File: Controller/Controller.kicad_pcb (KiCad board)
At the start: 2 copper layers, 30 x 213 mm, 93 parts, among them J1 CON_TLC, J2 CON_15V, J3 CON_ICSP, J4 DC out, J5 CON_5V, J6 CON_5V_AUX, J7 CON_USB_A, Q1 SI4435FDY, Q2 SI4435FDY, Q3 SQ2309ES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

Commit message: ...
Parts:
- moved F2 31.6 mm to (138.0, 174.5), turned to 270 degrees
- moved Q2 22.1 mm to (144.5, 175.0), turned to 90 degrees
- moved C1 20.5 mm to (143.5, 197.0), turned to 180 degrees
- moved D2 18.2 mm to (149.0, 174.5), turned to 270 degrees
- moved D1 15.6 mm to (151.5, 214.5)
- moved Q1 15.6 mm to (153.5, 219.5)
- moved R1 15.6 mm to (155.6, 214.5)
- moved R2 14.5 mm to (149.0, 178.0), turned to 270 degrees
- moved C2 14.2 mm to (143.5, 208.5), turned to 180 degrees
- moved R13 14.0 mm to (158.0, 44.0), turned to 0 degrees
- moved SW1 12.9 mm to (147.0, 37.0), turned to 270 degrees
- moved J5 12.3 mm to (138.5, 183.5)
- moved U4 11.2 mm to (158.0, 41.0), turned to 270 degrees
- moved C4 9.92 mm to (155.0, 175.0), turned to 0 degrees
- moved C24 9.43 mm to (158.0, 38.0), turned to 0 degrees
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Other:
- outline, holes or cut-outs redrawn

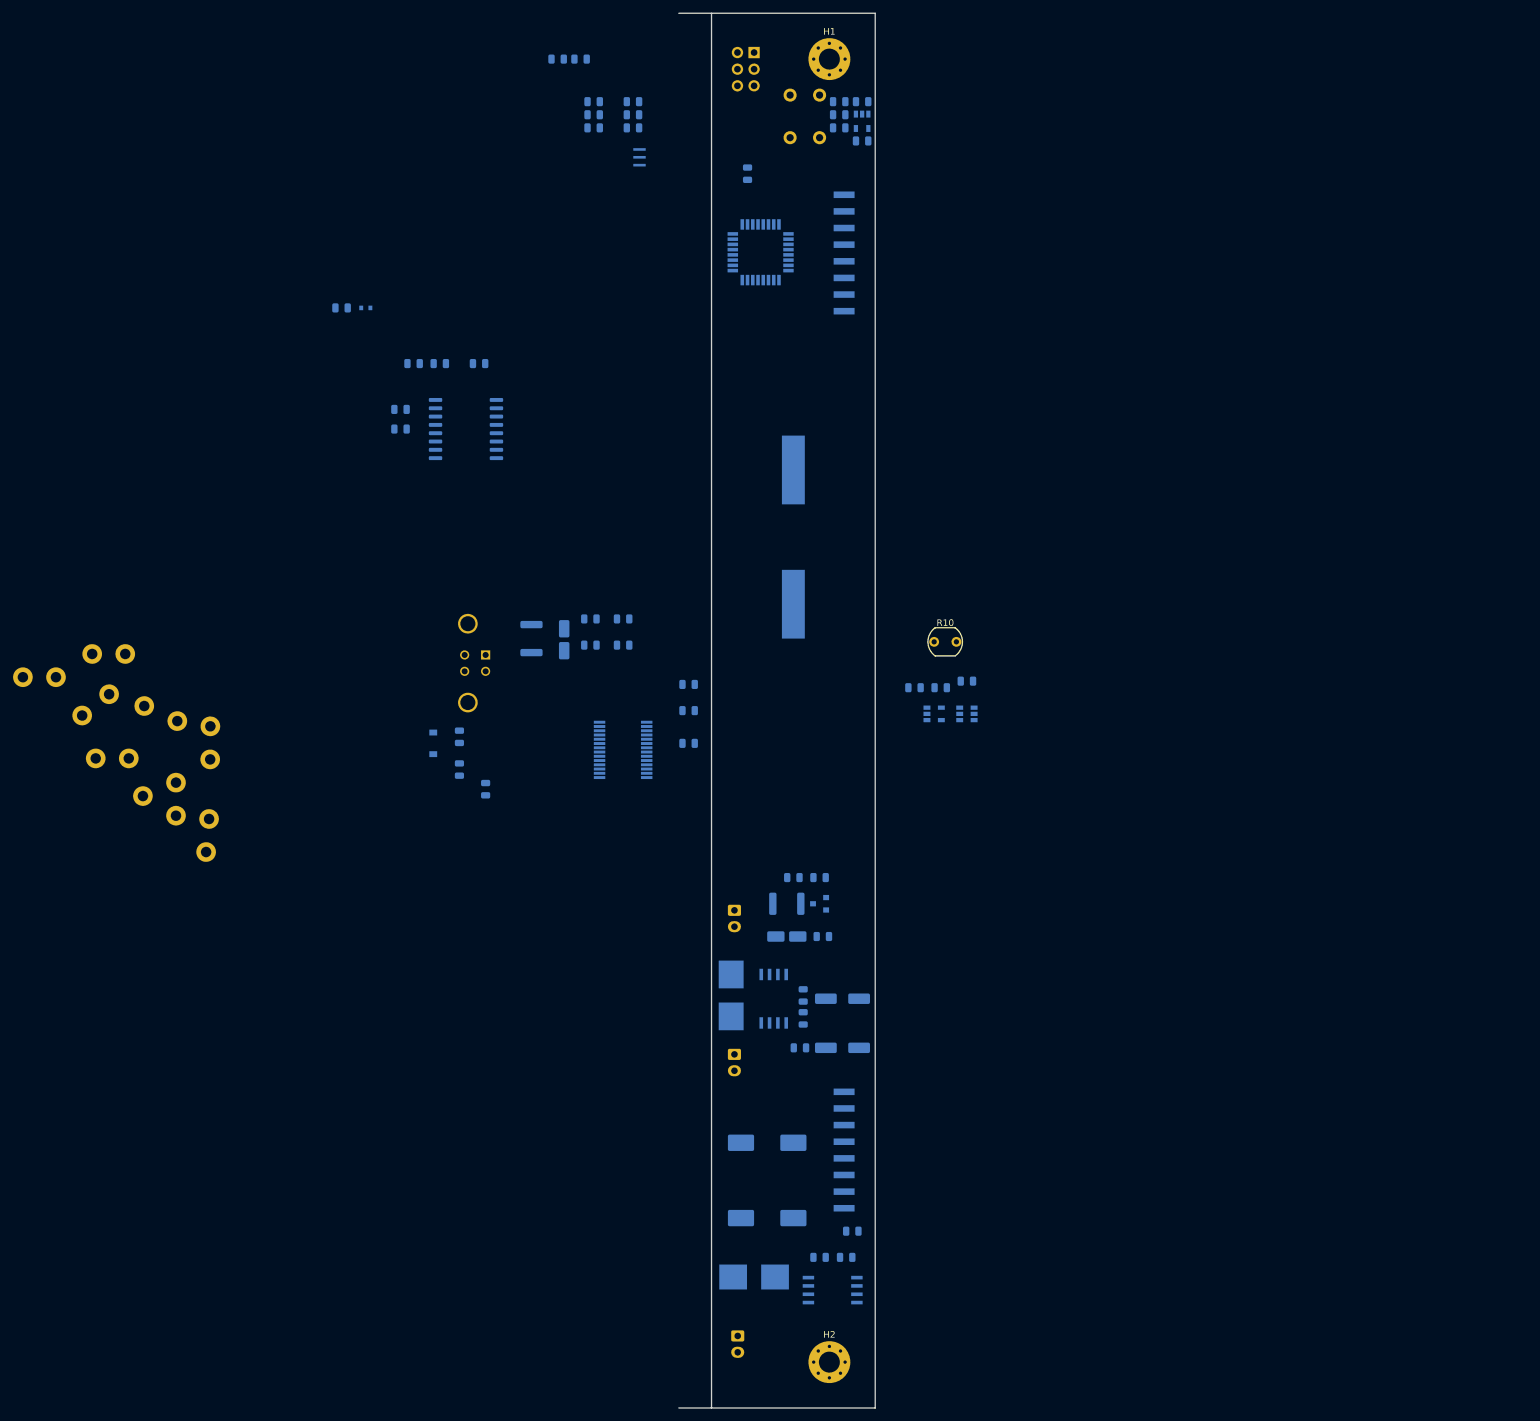
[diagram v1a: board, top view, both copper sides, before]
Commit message: Ground vias digit+colon. Placement/routing controller
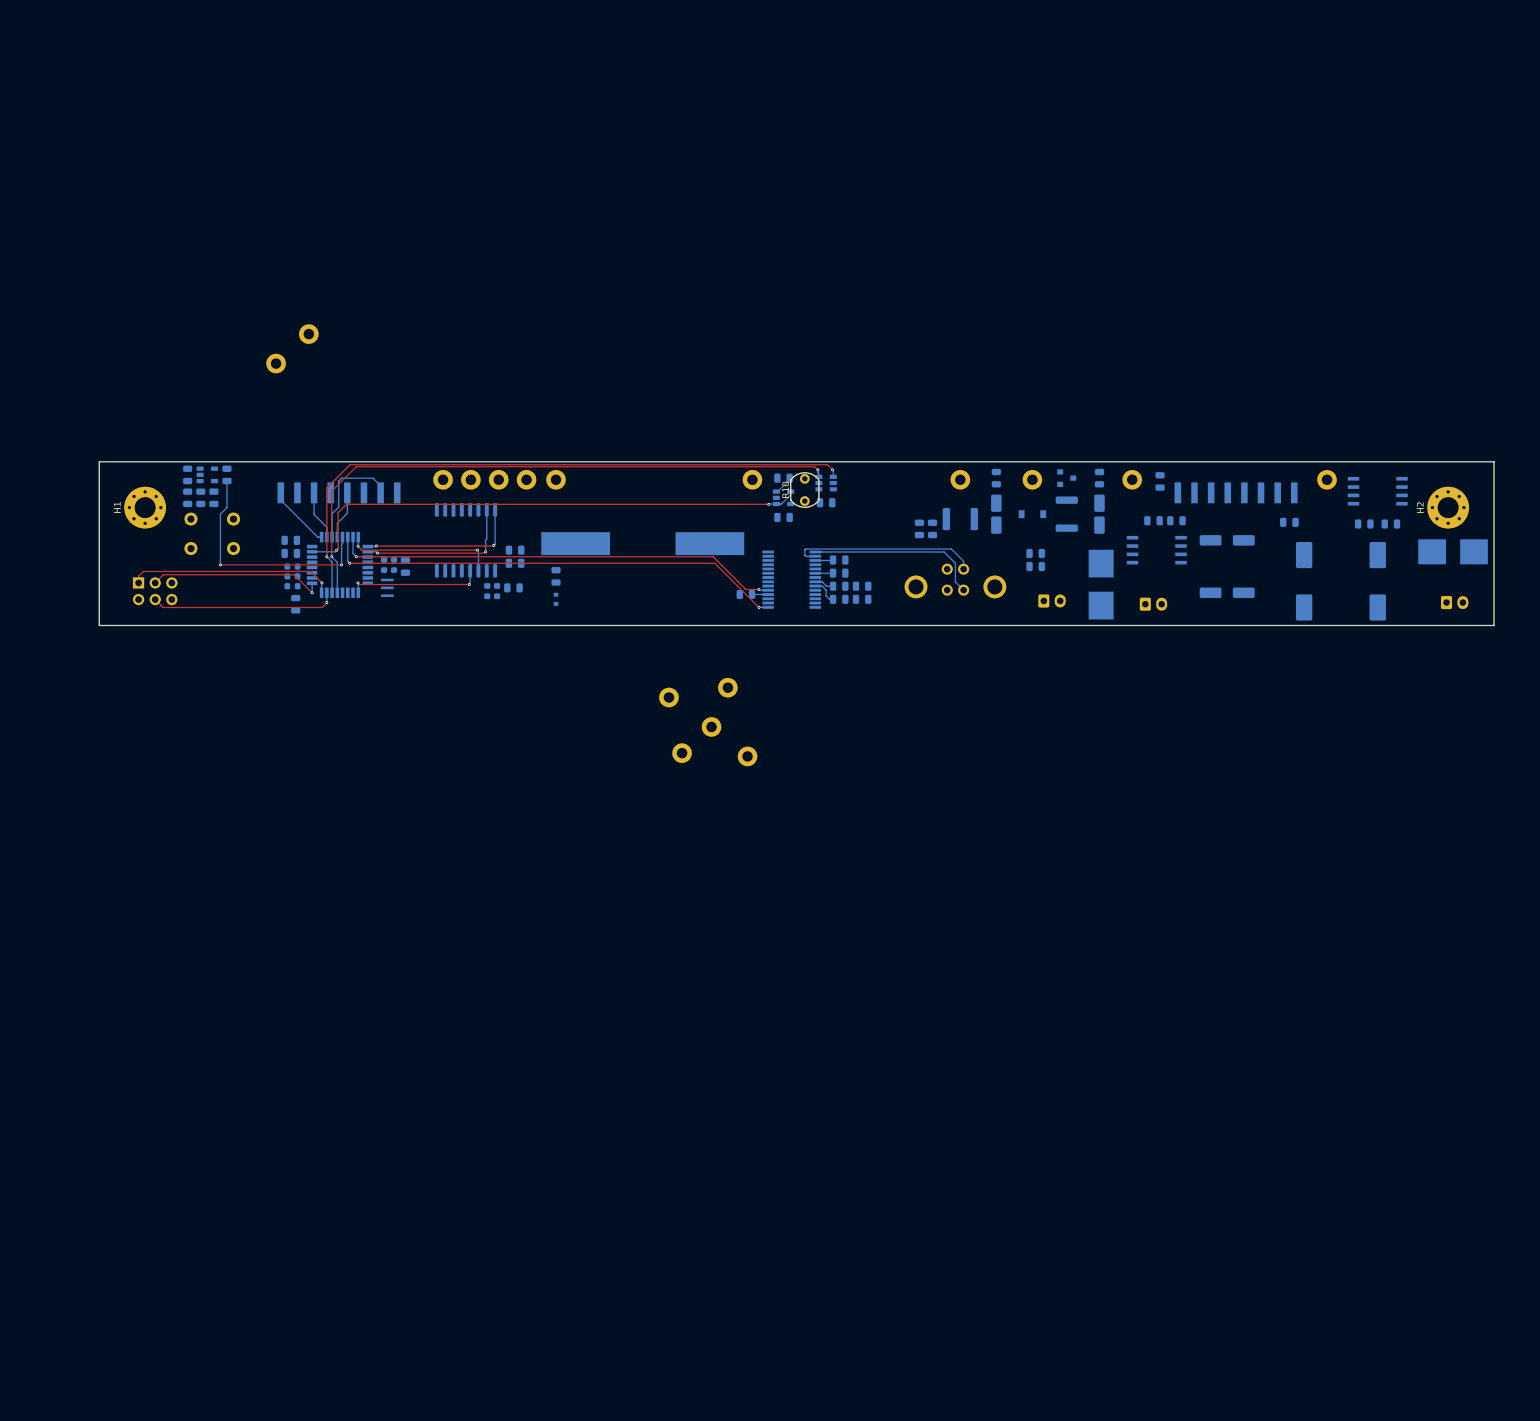
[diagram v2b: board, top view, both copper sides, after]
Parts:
- C14, C15, C16, C17, C18, C19, C20: footprint Capacitor_SMD:C_0805_2012Metric -> Capacitor_SMD:C_0603_1608Metric
- J7: footprint Connector_USB:USB_B_TE_5787834_Vertical -> ak:UJ2-BV-1-TH
- moved TP16 183.1 mm to (229.0, 95.8), turned to 90 degrees
- moved TP15 167.1 mm to (199.2, 95.8), turned to 90 degrees
- moved H2 161.1 mm to (247.5, 100.0), turned to 90 degrees
- moved J2 155.8 mm to (247.2, 114.5), turned to 0 degrees
- moved F1 153.8 mm to (248.2, 106.8)
- moved Q1 147.7 mm to (236.8, 97.5), turned to 0 degrees
- moved D1 142.0 mm to (238.8, 102.5), turned to 180 degrees
- moved R1 137.1 mm to (234.7, 102.5), turned to 180 degrees
- moved TP14 135.7 mm to (184.0, 95.8), turned to 90 degrees
- moved C2 134.7 mm to (236.8, 111.2), turned to 270 degrees
- moved J4 129.1 mm to (224.0, 97.8), turned to 180 degrees
- moved TP13 128.4 mm to (173.0, 95.8), turned to 90 degrees
- moved C3 127.2 mm to (223.2, 102.2), turned to 0 degrees
- moved H1 124.9 mm to (48.5, 100.0), turned to 90 degrees
- moved J3 124.1 mm to (47.5, 111.5), turned to 270 degrees
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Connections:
- U2 pad 12: /LED -> (no net)
- U2 pad 22: (no net) -> /LED
- U2 pad 24: /TLC_LAT -> (no net)
- U2 pad 26: (no net) -> /TLC_LAT
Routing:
- net /~POT_CS~: track 0.00 -> 96.5 mm, vias 0 -> 2
- net /POT_U~D~: track 0.00 -> 93.0 mm, vias 0 -> 2
- net /LDR: track 0.00 -> 80.4 mm, vias 0 -> 2
- net /FTDI_TX: track 0.00 -> 70.8 mm, vias 0 -> 2
- net /FTDI_RX: track 0.00 -> 68.2 mm, vias 0 -> 2
- net /~RESET~: track 0.00 -> 36.0 mm, vias 0 -> 2
- net /MISO: track 0.00 -> 31.6 mm, vias 0 -> 1
- net /USBD-: track 0.00 -> 28.8 mm
- net /MOSI: track 0.00 -> 28.5 mm, vias 0 -> 1
- net /SCK: track 0.00 -> 27.1 mm, vias 0 -> 1
- net /USBD+: track 0.00 -> 26.7 mm
- net /RTC_SCL: track 0.00 -> 24.8 mm, vias 0 -> 2
- net /RTC_SDA: track 0.00 -> 24.6 mm, vias 0 -> 2
- net /RTC_1PPS: track 0.00 -> 23.1 mm, vias 0 -> 2
- net /~RTC_RST~: track 0.00 -> 20.8 mm, vias 0 -> 2
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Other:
- board size 30 x 213 mm -> 213 x 25 mm
- net class Default: clearance 0.2 -> 0.15; trace_width 0.25 -> 0.15
- rule solder_mask_min_width: 0.25 -> 0.05
- rule trace_clearance: 0.2 -> 0.15
- rule trace_min: 0.2 -> 0.15
- rule via_min_drill: 0.3 -> 0.2
- rule via_min_size: 0.4 -> 0.45

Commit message: Routing controller
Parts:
- added R15: 47k, Resistor_SMD:R_0603_1608Metric, B.Cu at (166.4, 97.8)
- C10, C12, C13, C21, C22, C23, C24, C25, C6, C7, C8: footprint Capacitor_SMD:C_0805_2012Metric -> Capacitor_SMD:C_0603_1608Metric
- D1, D2, D4, D5, D6, D7, D8: footprint LED_SMD:LED_0805_2012Metric -> LED_SMD:LED_0603_1608Metric
- D9: value BAS716 -> SS1P3L; footprint Diode_SMD:D_SOD-523 -> Diode_SMD:D_SOD-123
- R1, R11, R12, R13, R14, R2, R3, R4, R5, R6, R7, R8, R9: footprint Resistor_SMD:R_0805_2012Metric -> Resistor_SMD:R_0603_1608Metric
- moved TP11 32.7 mm to (95.8, 96.0)
- moved TP10 28.8 mm to (91.5, 96.0)
- moved C23 18.9 mm to (164.8, 97.8), turned to 270 degrees
- moved L1 18.2 mm to (88.8, 109.0)
- moved L2 17.4 mm to (71.8, 114.5)
- moved R10 17.3 mm to (165.0, 106.2)
- moved U5 16.3 mm to (162.0, 101.5), turned to 180 degrees
- moved C14 15.6 mm to (71.0, 110.5), turned to 0 degrees
- moved C16 15.6 mm to (86.5, 108.8), turned to 90 degrees
- moved TP5 14.1 mm to (155.2, 97.8)
- moved C22 13.2 mm to (159.2, 101.5), turned to 270 degrees
- moved SW1 12.4 mm to (65.8, 113.2), turned to 90 degrees
- moved TP9 10.3 mm to (104.2, 96.0)
- moved TP14 10.2 mm to (194.2, 95.8)
- moved U6 9.62 mm to (162.0, 97.8)
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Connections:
- C21 pad 1: +3V3 -> +5V
- C23 pad 1: GND -> Net-(C23-Pad1)
- R11 pad 2: +3V3 -> +5V
- U2 pad 13: /POT_U~D~ -> /~POT_CS~
- U2 pad 14: /~POT_CS~ -> /POT_U~D~
- U4 pad 5: +3V3 -> +5V
- U6 pad 5: GND -> Net-(C23-Pad1)
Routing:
- net +5V: track 5.20 -> 360.7 mm, vias 0 -> 11
- net GND: track 0.00 -> 36.0 mm, vias 0 -> 17
- net /TLC_BLANK: track 9.67 -> 41.6 mm
- net /TLC_SCL: track 7.38 -> 34.0 mm
- net /RTC_32K: track 0.00 -> 23.8 mm
- net /TLC_LAT: track 7.56 -> 27.6 mm
- net /TLC_SDA: track 17.1 -> 37.0 mm
- net /~RESET~: track 36.0 -> 21.6 mm
- net VBUS: track 0.00 -> 13.5 mm
- net /FTDI_TX: track 70.8 -> 83.6 mm
- net /LDR: track 80.4 -> 92.7 mm
- net Net-(R11-Pad1): track 0.00 -> 11.5 mm
- net /FTDI_RX: track 68.2 -> 79.2 mm
- net /POT_U~D~: track 93.0 -> 100.5 mm
- net Net-(C14-Pad2): track 0.00 -> 7.05 mm
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- added copper zone on B.Cu, net GND
- added copper zone on F.Cu, net GND
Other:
- net class Default: clearance 0.15 -> 0.2; trace_width 0.15 -> 0.2; via_dia 0.8 -> 0.45; via_drill 0.4 -> 0.2
- rule trace_clearance: 0.15 -> 0.2

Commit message: ...
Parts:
- moved R8 7.42 mm to (104.8, 106.5), turned to 180 degrees
- moved R9 5.37 mm to (104.8, 105.0), turned to 180 degrees
- moved L3 2.37 mm to (102.5, 114.2), turned to 90 degrees
- moved C19 2.34 mm to (99.2, 114.0)
- moved C20 2.34 mm to (100.7, 114.0)
- moved U3 1.75 mm to (97.5, 106.2)
- moved R10 1.50 mm to (166.5, 106.2), turned to 180 degrees
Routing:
- net +5V: track 360.7 -> 387.3 mm, vias 11 -> 2
- net Net-(F3-Pad2): track 0.00 -> 5.86 mm
- net Net-(C19-Pad2): track 5.47 -> 0.00 mm
- net GND: track 36.0 -> 30.7 mm, vias 17 -> 16
- net Net-(C23-Pad2): track 8.22 -> 3.50 mm
- net /~RESET~: track 21.6 -> 16.9 mm
- net /RTC_SDA: track 24.0 -> 26.6 mm
- net /RTC_32K: track 23.8 -> 21.7 mm
- net Net-(D4-Pad2): track 0.00 -> 2.00 mm
- net /LDR: track 92.7 -> 94.6 mm
- net /RTC_1PPS: track 26.6 -> 24.9 mm
- net /RTC_SCL: track 24.0 -> 25.6 mm
- net /~POT_CS~: track 100.5 -> 98.9 mm
- net /POT_U~D~: track 100.5 -> 99.0 mm
- net /FTDI_TX: track 83.6 -> 82.8 mm

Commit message: layout...
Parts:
- moved TP17 90.7 mm to (230.0, 123.5)
- moved TP2 28.6 mm to (112.8, 113.2)
- moved TP8 26.7 mm to (107.0, 113.2)
- moved R8 19.0 mm to (85.8, 106.5)
- moved R9 19.0 mm to (85.8, 105.0)
- moved R15 7.43 mm to (159.1, 99.2), turned to 270 degrees
- moved C25 7.14 mm to (166.2, 99.2), turned to 270 degrees
- moved C23 4.33 mm to (160.7, 99.2), turned to 90 degrees
- moved D5 3.29 mm to (168.2, 103.0)
- moved R10 3.29 mm to (163.2, 106.8), turned to 0 degrees
- moved C22 2.70 mm to (160.8, 103.8), turned to 90 degrees
- moved U5 2.30 mm to (163.5, 103.2), turned to 270 degrees
- moved U6 2.12 mm to (163.5, 99.2), turned to 180 degrees
- moved TP5 2.00 mm to (155.2, 95.8)
- moved R4 1.25 mm to (170.0, 103.0), turned to 90 degrees
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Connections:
- U2 pad 13: /~POT_CS~ -> /POT_U~D~
- U2 pad 14: /POT_U~D~ -> /~POT_CS~
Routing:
- net +5V: track 387.3 -> 319.4 mm
- net +BATT: track 2.46 -> 40.5 mm, vias 0 -> 2
- net /RTC_1PPS: track 24.9 -> 44.1 mm, vias 2 -> 3
- net /LDR: track 94.6 -> 109.9 mm
- net Net-(C23-Pad2): track 3.50 -> 12.8 mm
- net VBUS: track 13.5 -> 22.0 mm
- net Net-(C19-Pad2): track 0.00 -> 5.66 mm
- net /RTC_32K: track 21.7 -> 26.9 mm, vias 0 -> 2
- net /~POT_CS~: track 98.9 -> 94.8 mm
- net /POT_U~D~: track 99.0 -> 96.3 mm
- net /RTC_SDA: track 26.6 -> 24.4 mm
- net Net-(D5-Pad2): track 0.00 -> 1.75 mm
- net /RTC_SCL: track 25.6 -> 24.4 mm
- net /TLC_SCL: vias 0 -> 1

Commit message: Finished routing controller pcb.
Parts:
- removed TP17, TP6: TestPoint_Alt, TestPoint:TestPoint_Loop_D2.60mm_Drill1.6mm_Beaded
- removed the TP4 at (135.0, 133.5)
- moved SW1 1.35 mm to (64.4, 113.2)
- moved C6 0.25 mm to (203.5, 95.8)
- moved D1 0.25 mm to (237.0, 101.8)
- moved R1 0.25 mm to (233.8, 101.8)
- renumbered TP8 to TP4
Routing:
- net Net-(F1-Pad2): track 0.00 -> 10.2 mm
- net Net-(F2-Pad2): track 0.00 -> 7.33 mm
- net GND: track 30.3 -> 34.8 mm, vias 16 -> 151
- net Net-(C16-Pad2): track 6.45 -> 10.4 mm
- net /FTDI_RX: track 78.9 -> 81.1 mm
- net /FTDI_TX: track 82.8 -> 84.6 mm
- net +5V: track 319.4 -> 317.7 mm
- net Net-(D2-Pad2): track 0.00 -> 1.68 mm
- net Net-(D1-Pad2): track 0.00 -> 1.68 mm
- net Net-(D8-Pad2): track 0.00 -> 1.50 mm
- net Net-(R11-Pad1): track 11.5 -> 12.2 mm
- added copper zone on B.Cu, net +15V
- added copper zone on B.Cu, net +5VD
- added copper zone on B.Cu, net Net-(F1-Pad1)
- added copper zone on B.Cu, net Net-(F2-Pad1)
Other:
- board text added: "+15V"
- board text added: "+5V"
- board text added: "+5Vd"
- board text added: "1PPS"
- board text added: "32K"
- board text added: "BLANK"
- board text added: "ISP"
- board text added: "LAT"
- board text added: "LDR"
- board text added: "RESET"
- board text added: "SCL"
- board text added: "SDA"
- board text added: "VBAT"
- board text added: "VBUS"

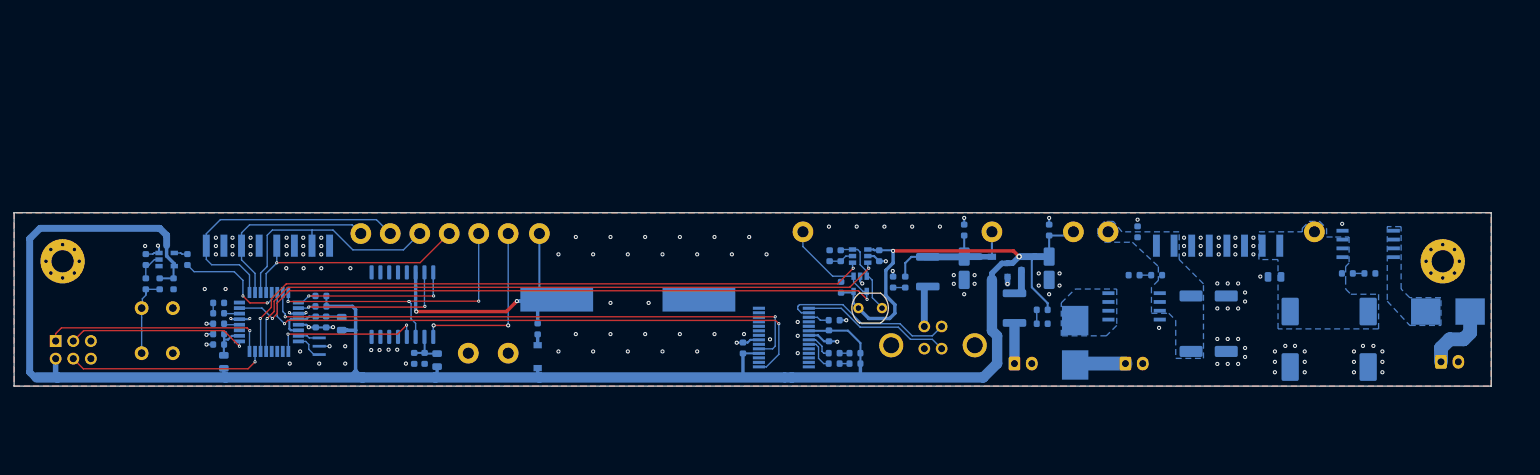
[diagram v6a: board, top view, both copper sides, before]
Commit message: Moved mounting holes. Moved stuff around on controller PCB.
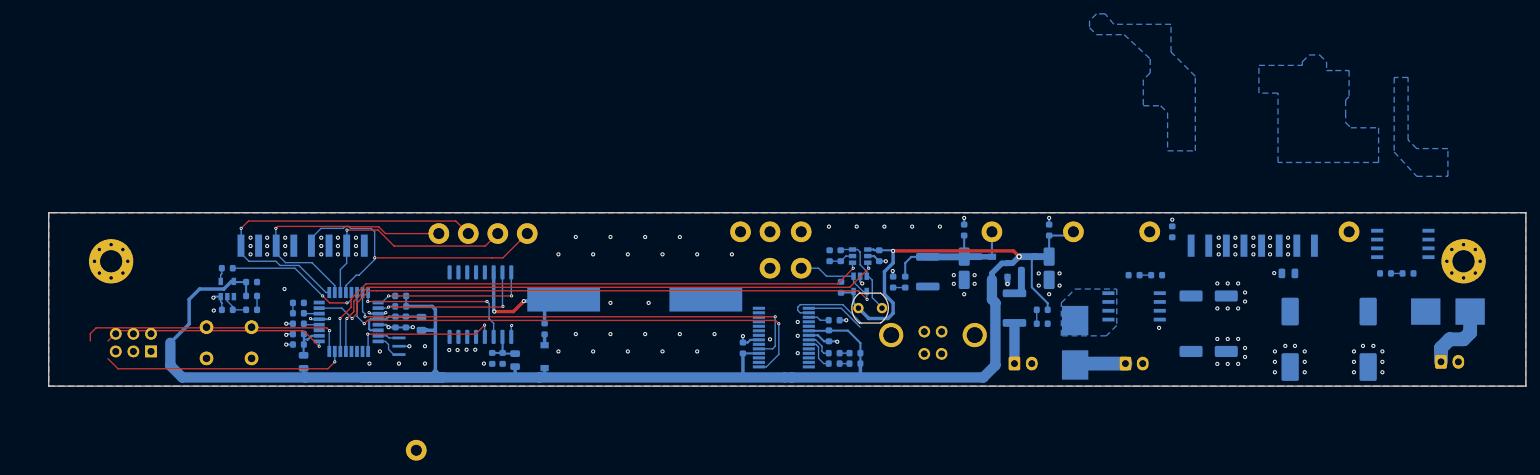
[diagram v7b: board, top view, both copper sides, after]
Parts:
- F3, F4: footprint Fuse:Fuse_1812_4532Metric -> ak:Fuse_1812_4532Metric
- moved TP2 39.7 mm to (150.5, 101.0)
- moved TP1 37.8 mm to (146.2, 95.8)
- moved TP12 37.8 mm to (155.0, 95.8)
- moved TP3 37.8 mm to (150.5, 95.8)
- moved TP4 15.9 mm to (99.5, 127.2)
- moved R12 15.7 mm to (75.8, 107.0), turned to 0 degrees
- moved J3 13.8 mm to (61.2, 113.0), turned to 90 degrees
- moved C24 13.8 mm to (72.2, 107.0), turned to 180 degrees
- moved R11 13.4 mm to (75.8, 105.0), turned to 180 degrees
- moved C14 11.5 mm to (82.5, 110.5)
- moved C15 11.5 mm to (82.5, 112.0)
- moved C16 11.5 mm to (98.0, 108.8)
- moved C17 11.5 mm to (96.5, 108.8)
- moved C18 11.5 mm to (82.5, 109.0)
- moved D8 11.5 mm to (82.5, 106.0)
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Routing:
- net +5V: track 317.7 -> 279.3 mm
- net /RTC_32K: track 26.9 -> 1.67 mm, vias 2 -> 1
- net +BATT: track 40.5 -> 15.8 mm
- net /RTC_1PPS: track 44.2 -> 24.2 mm, vias 3 -> 2
- net /LDR: track 109.9 -> 95.2 mm
- net /USBD+: track 21.6 -> 8.53 mm
- net /USBD-: track 25.5 -> 12.7 mm
- net /POT_U~D~: track 96.3 -> 84.8 mm
- net /FTDI_TX: track 84.6 -> 73.1 mm
- net /FTDI_RX: track 81.1 -> 69.6 mm
- net /~POT_CS~: track 94.8 -> 83.3 mm
- net /TLC_LAT: track 27.6 -> 39.0 mm, vias 0 -> 1
- net /TLC_SCL: track 34.0 -> 45.4 mm
- net /TLC_BLANK: track 41.6 -> 52.6 mm, vias 0 -> 1
- net Net-(R11-Pad1): track 12.2 -> 2.00 mm
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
